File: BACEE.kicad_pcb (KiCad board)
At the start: 2 copper layers, 0 parts

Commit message: Set design rules.
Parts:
- added BT1: Battery 3V, Connector_PinHeader_2.54mm:PinHeader_1x02_P2.54mm_Vertical, F.Cu at (101.1, 87.5)
- added C1: C22pF, Capacitor_SMD:C_0805_2012Metric_Pad1.15x1.40mm_HandSolder, F.Cu at (154.9, 96.5)
- added C2: C22pF, Capacitor_SMD:C_0805_2012Metric_Pad1.15x1.40mm_HandSolder, F.Cu at (155.0, 102.4)
- added C3: 10uF, Capacitor_SMD:C_0805_2012Metric_Pad1.15x1.40mm_HandSolder, F.Cu at (148.8, 106.7)
- added D1: LED, LED_SMD:LED_0805_2012Metric_Pad1.15x1.40mm_HandSolder, F.Cu at (144.0, 105.6)
- added J1: Serial, Connector_PinSocket_2.54mm:PinSocket_1x04_P2.54mm_Vertical, F.Cu at (89.4, 87.6)
- added J2: Digital pins, Connector_PinSocket_2.54mm:PinSocket_1x09_P2.54mm_Vertical, F.Cu at (80.2, 87.6)
- added J3: ICSP, Connector_PinSocket_2.54mm:PinSocket_2x03_P2.54mm_Vertical, F.Cu at (96.5, 87.6)
- added J4: I2C, Connector_PinSocket_2.54mm:PinSocket_1x04_P2.54mm_Vertical, F.Cu at (84.8, 87.6)
- added R1: 330Ohm, Resistor_SMD:R_0805_2012Metric_Pad1.15x1.40mm_HandSolder, F.Cu at (154.9, 99.5)
- added R2: 10KOhm, Resistor_SMD:R_0805_2012Metric_Pad1.15x1.40mm_HandSolder, F.Cu at (150.2, 103.7)
- added U1: DS1337S+, Package_SO:SOIJ-8_5.3x5.3mm_P1.27mm, F.Cu at (142.6, 100.6)
- added U2: 24LC1025, Package_SO:SOIJ-8_5.3x5.3mm_P1.27mm, F.Cu at (142.6, 93.7)
- added U3: 24LC1025, Package_SO:SO-8_5.3x6.2mm_P1.27mm, F.Cu at (131.2, 105.5)
- added U4: ATMEGA328P-AU, digikey-footprints:TQFP-32_7x7mm, F.Cu at (131.6, 95.9)
- added Y1: Crystal 32MHz, Crystal:Crystal_SMD_MicroCrystal_CC7V-T1A-2Pin_3.2x1.5mm, F.Cu at (139.1, 105.8)
- added Y2: Crystal 16MHz, Crystal:Crystal_SMD_5032-2Pin_5.0x3.2mm_HandSoldering, F.Cu at (153.0, 92.6)
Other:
- net class Power added: clearance 0.2, trace_width 0.3, via_dia 1, via_drill 0.6

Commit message: Placement complete
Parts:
- moved Y2 62.2 mm to (93.7, 111.4)
- moved R2 59.3 mm to (91.0, 108.0), turned to 180 degrees
- moved C1 56.2 mm to (101.2, 113.0)
- moved C2 54.3 mm to (101.2, 110.4)
- moved R1 44.6 mm to (117.5, 123.7), turned to 180 degrees
- moved J2 43.9 mm to (95.4, 128.8), turned to 90 degrees
- moved U4 43.0 mm to (96.0, 120.0)
- moved U2 39.5 mm to (108.6, 113.8)
- moved U1 39.3 mm to (108.6, 120.3)
- moved J4 34.3 mm to (113.9, 105.7), turned to 90 degrees
- moved C3 33.7 mm to (117.5, 119.3), turned to 180 degrees
- moved J3 31.9 mm to (88.1, 118.4)
- moved D1 28.8 mm to (121.7, 123.7)
- moved BT1 27.0 mm to (85.6, 109.6)
- moved Y1 22.0 mm to (121.6, 119.3)
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
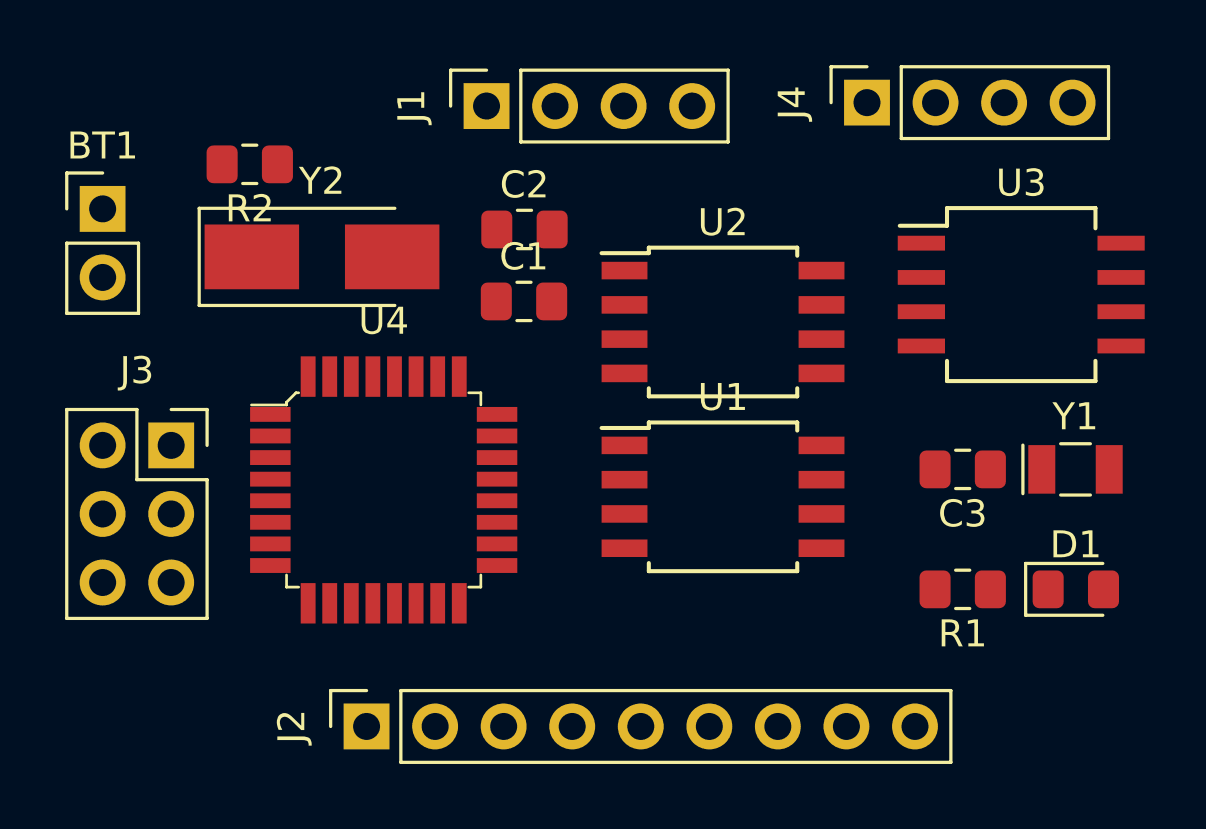
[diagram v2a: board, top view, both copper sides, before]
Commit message: Compleated Outlines and mounting holes
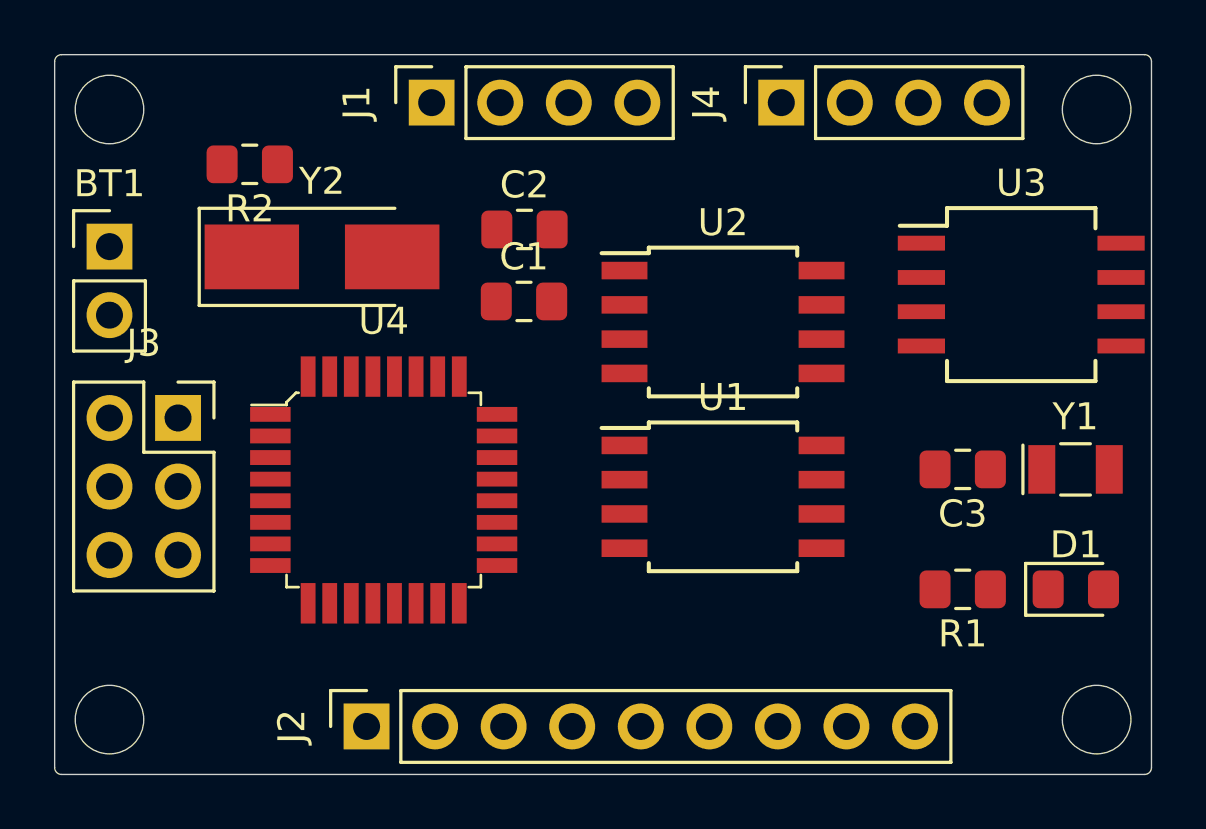
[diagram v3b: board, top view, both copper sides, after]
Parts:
- moved J4 3.17 mm to (110.7, 105.7)
- moved J1 2.04 mm to (97.8, 105.7)
- moved BT1 1.42 mm to (85.9, 111.0)
- moved J3 1.05 mm to (88.4, 117.3)
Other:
- board outline added: 40.6 x 26.7 mm
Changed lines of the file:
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@@
   (general
     (thickness 1.6)
-    (drawings 0)
+    (drawings 12)
     (tracks 0)
     (zones 0)
@@
   )
   (module Connector_PinHeader_2.54mm:PinHeader_1x02_P2.54mm_Vertical (layer F.Cu)
-    (at 85.598 109.601)
+    (at 85.852 110.998)
     (descr "Through hole straight pin header, 1x02, 2.54mm pitch, single row")
     (tags "Through hole pin header THT 1x02 2.54mm single row")
@@
   )
   (module Connector_PinSocket_2.54mm:PinSocket_1x04_P2.54mm_Vertical (layer F.Cu)
-    (at 99.822 105.791 90)
+    (at 97.79 105.664 90)
     (descr "Through hole straight socket strip, 1x04, 2.54mm pitch, single row (from Kicad 4.0.7), script generated")
     (tags "Through hole socket strip THT 1x04 2.54mm single row")
@@
   )
   (module Connector_PinSocket_2.54mm:PinSocket_2x03_P2.54mm_Vertical (layer F.Cu)
-    (at 88.138 118.364)
+    (at 88.392 117.348)
     (descr "Through hole straight socket strip, 2x03, 2.54mm pitch, double cols (from Kicad 4.0.7), script generated")
     (tags "Through hole socket strip THT 2x03 2.54mm double row")
@@
   )
   (module Connector_PinSocket_2.54mm:PinSocket_1x04_P2.54mm_Vertical (layer F.Cu)
-    (at 113.919 105.664 90)
+    (at 110.744 105.664 90)
     (descr "Through hole straight socket strip, 1x04, 2.54mm pitch, single row (from Kicad 4.0.7), script generated")
     (tags "Through hole socket strip THT 1x04 2.54mm single row")
@@
     )
   )
+  (gr_circle (center 122.428 105.918) (end 121.158 105.918) (layer Edge.Cuts) (width 0.05))
+  (gr_circle (center 122.428 128.524) (end 121.158 128.524) (layer Edge.Cuts) (width 0.05))
+  (gr_circle (center 85.852 128.524) (end 84.582 128.524) (layer Edge.Cuts) (width 0.05))
+  (gr_circle (center 85.852 105.918) (end 84.582 105.918) (layer Edge.Cuts) (width 0.05))
+  (gr_line (start 83.82 130.302) (end 83.82 104.14) (layer Edge.Cuts) (width 0.05))
+  (gr_line (start 124.206 130.556) (end 84.074 130.556) (layer Edge.Cuts) (width 0.05))
+  (gr_line (start 124.46 104.14) (end 124.46 130.302) (layer Edge.Cuts) (width 0.05))
+  (gr_line (start 84.074 103.886) (end 124.206 103.886) (layer Edge.Cuts) (width 0.05))
+  (gr_arc (start 124.206 104.14) (end 124.46 104.14) (angle -90) (layer Edge.Cuts) (width 0.05))
+  (gr_arc (start 124.206 130.302) (end 124.206 130.556) (angle -90) (layer Edge.Cuts) (width 0.05))
+  (gr_arc (start 84.074 130.302) (end 83.82 130.302) (angle -90) (layer Edge.Cuts) (width 0.05))
+  (gr_arc (start 84.074 104.14) (end 84.074 103.886) (angle -90) (layer Edge.Cuts) (width 0.05))
 )

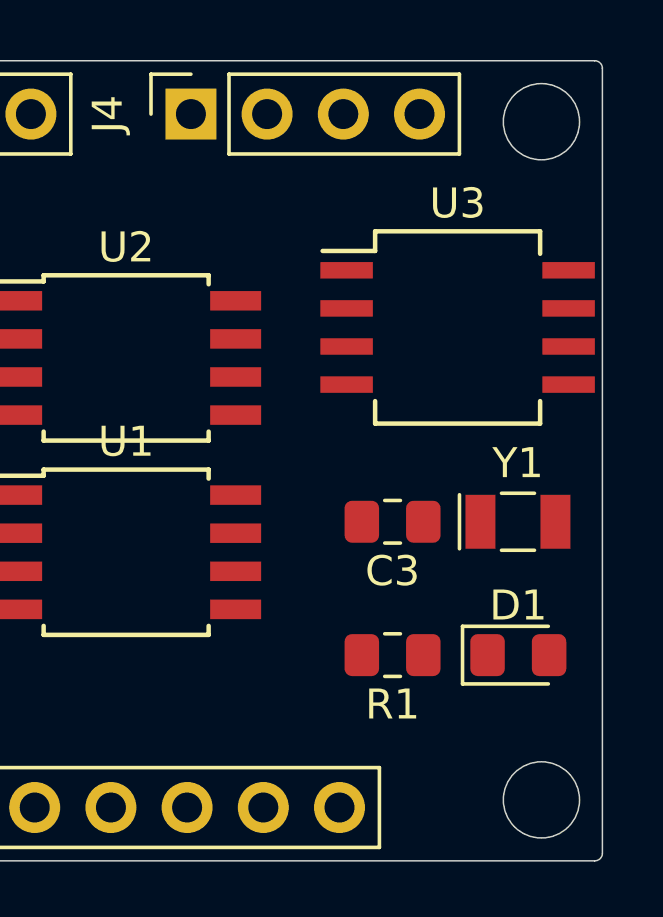
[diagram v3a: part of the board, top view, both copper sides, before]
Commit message: Compleated Outlines and mounting holes, corrected
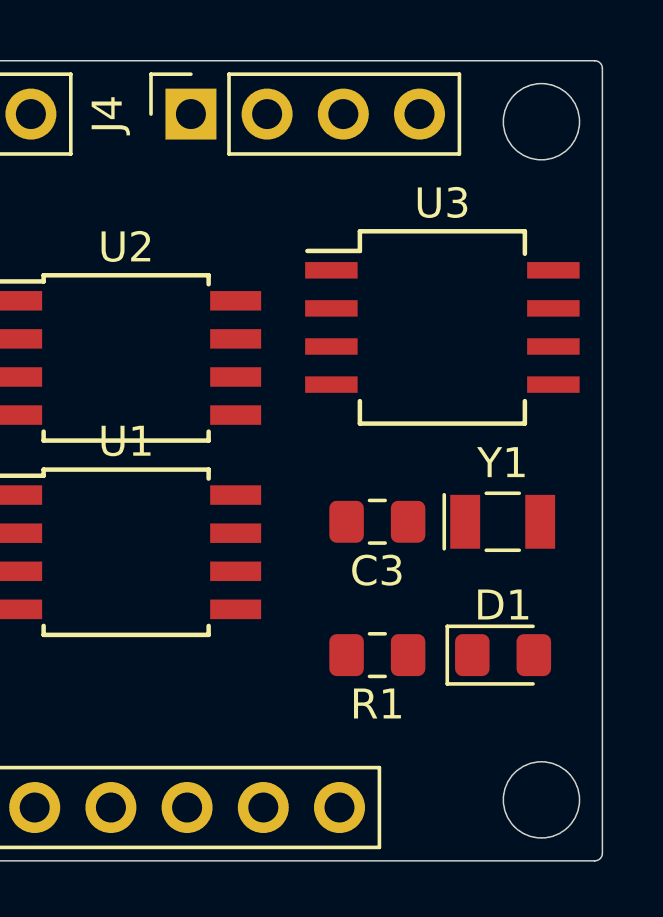
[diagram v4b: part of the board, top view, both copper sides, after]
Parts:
- moved C3 0.51 mm to (117.0, 119.3)
- moved D1 0.51 mm to (121.1, 123.7)
- moved R1 0.51 mm to (117.0, 123.7)
- moved U3 0.51 mm to (119.1, 112.8)
- moved Y1 0.51 mm to (121.1, 119.3)
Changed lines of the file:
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@@
   )
   (module Capacitor_SMD:C_0805_2012Metric_Pad1.15x1.40mm_HandSolder (layer F.Cu)
-    (at 117.466 119.253 180)
+    (at 116.958 119.253 180)
     (descr "Capacitor SMD 0805 (2012 Metric), square (rectangular) end terminal, IPC_7351 nominal with elongated pad for handsoldering. (Body size source: https://docs.google.com/spreadsheets/d/1BsfQQcO9C6DZCsRaXUlFlo91Tg2WpOkGARC1WS5S8t0/edit?usp=sharing), generated with kicad-footprint-generator")
     (tags "capacitor handsolder")
@@
   )
   (module LED_SMD:LED_0805_2012Metric_Pad1.15x1.40mm_HandSolder (layer F.Cu)
-    (at 121.657 123.698)
+    (at 121.149 123.698)
     (descr "LED SMD 0805 (2012 Metric), square (rectangular) end terminal, IPC_7351 nominal, (Body size source: https://docs.google.com/spreadsheets/d/1BsfQQcO9C6DZCsRaXUlFlo91Tg2WpOkGARC1WS5S8t0/edit?usp=sharing), generated with kicad-footprint-generator")
     (tags "LED handsolder")
@@
   )
   (module Resistor_SMD:R_0805_2012Metric_Pad1.15x1.40mm_HandSolder (layer F.Cu)
-    (at 117.466 123.698 180)
+    (at 116.958 123.698 180)
     (descr "Resistor SMD 0805 (2012 Metric), square (rectangular) end terminal, IPC_7351 nominal with elongated pad for handsoldering. (Body size source: https://docs.google.com/spreadsheets/d/1BsfQQcO9C6DZCsRaXUlFlo91Tg2WpOkGARC1WS5S8t0/edit?usp=sharing), generated with kicad-footprint-generator")
     (tags "resistor handsolder")
@@
   )
   (module Package_SO:SO-8_5.3x6.2mm_P1.27mm (layer F.Cu)
-    (at 119.634 112.776)
+    (at 119.126 112.776)
     (descr "8-Lead Plastic Small Outline, 5.3x6.2mm Body (http://www.ti.com.cn/cn/lit/ds/symlink/tl7705a.pdf)")
     (tags "SOIC 1.27")
@@
   )
   (module Crystal:Crystal_SMD_MicroCrystal_CC7V-T1A-2Pin_3.2x1.5mm (layer F.Cu)
-    (at 121.646 119.253)
+    (at 121.138 119.253)
     (descr "SMD Crystal MicroCrystal CC7V-T1A/CM7V-T1A series https://www.microcrystal.com/fileadmin/Media/Products/32kHz/Datasheet/CC7V-T1A.pdf, 3.2x1.5mm^2 package")
     (tags "SMD SMT crystal")
